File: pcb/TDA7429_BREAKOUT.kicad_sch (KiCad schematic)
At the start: 53 parts

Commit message: start redesigning schematic
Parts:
- removed AUDIO_IN: (no value), symbol pinhead:PINHD-2X6
- removed AUDIO_OUT: (no value), symbol pinhead:PINHD-2X4
- removed C1, C15, C17, C2: 22nF, symbol OPL Eagle Library:C*-0805
- removed C10, C8, C9: 2.2uF, symbol OPL Eagle Library:C*-0805
- removed C11, C12, C13, C14, C30, C4: 100nF, symbol OPL Eagle Library:C*-0805
- removed C16, C18: 18nF, symbol OPL Eagle Library:C*-0805
- removed C19, C20, C6: 5.6nF, symbol OPL Eagle Library:C*-0805
- removed C21: 22uF, symbol OPL Eagle Library:C*-0805
- removed C22, C23, C24, C25, C26, C27: 0.47uF, symbol OPL Eagle Library:C*-0805
- removed C3: 4.7nF, symbol OPL Eagle Library:C*-0805
- removed C31: 10uF, symbol OPL Eagle Library:C*-0805
- removed C5: 1.2nF, symbol OPL Eagle Library:C*-0805
- removed C7: 680nF, symbol OPL Eagle Library:C*-0805
- removed D1: (no value), symbol OPL Eagle Library:LED*
- removed DATA, POWER: (no value), symbol SparkFun-Connectors:M02PTH
- removed FRAME1 (x2): (no value), symbol SparkFun-Aesthetics:FRAME-LETTER
- removed GND1, GND10, GND11, GND12, GND13, GND14, GND15, GND17, GND20, GND21: (no value), symbol supply1:GND
- removed MONITOR: (no value), symbol pinhead:PINHD-2X2
- removed R1, R2: 5.6K, symbol OPL Eagle Library:R*-0603
- removed R3, R4: 2.7K, symbol OPL Eagle Library:R*-0603
- removed R5: 220, symbol OPL Eagle Library:R*-0603
- removed TDA7429S: (no value), symbol ATK_lib:TDA7429S_SURFACE
- added C1, C10, C11, C12, C13, C14, C15, C16, C17, C18, C19, C2, C20, C21, C22, C23, C24, C25, C26, C27, C28, C29, C3, C4, C5, C6, C7, C8, C9: 22nF, symbol Device:C_Small
- added R1, R2: 2.7K, symbol Device:R_Small
- added R3: R_Small, symbol Device:R_Small
- added R4: 5.6K, symbol Device:R_Small
- added U1: TDA7429S, TDA7429:SDIP-42_W15.24mm_P1.778mm, symbol TDA7429:TDA7429S_TC
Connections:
- new net: C16.1, C17.1, R4.1
- new net: C17.2, U1.15 (BASS_LO)
- new net: C19.2, C20.2, U1.42 (V_S)
- new net: C10.1, C9.1, R1.1
- new net: C9.2, U1.19 (MIDDLE_LO)
- new net: C11.1, C12.1, R2.1
- new net: C11.2, U1.21 (MIDDLE_RO)
- new net: C26.2, U1.40 (R_IN3)
- new net: C12.2, U1.22 (MIDDLE_RI)
- new net: C14.1, C15.1, R3.1
- new net: C16.2, U1.16 (BASS_LI)
- new net: C27.1, U1.10 (REARIN)
- new net: C27.2, U1.9 (REAROUT)
- new net: C29.1, U1.13 (VAR_R)
- new net: C29.2, U1.14 (BASSO_R)
- new net: C1.2, U1.1 (PS4)
- new net: C7.2, U1.23 (TREBLE_R)
- new net: C4.2, U1.4 (PS1)
- new net: C23.2, U1.35 (L_IN1)
- new net: C10.2, U1.20 (MIDDLE_LI)
- new net: C15.2, U1.17 (BASS_RO)
- new net: C18.2, U1.41 (CREF)
- new net: C8.2, U1.24 (TREBLE_L)
- new net: C14.2, U1.18 (BASS_RI)
- new net: C28.1, U1.11 (VAR_L)
- new net: C28.2, U1.12 (BASSO_L)
- new net: C2.2, U1.2 (PS3)
- new net: C3.2, U1.3 (PS2)
- new net: C21.2, U1.33 (L_IN3)
- new net: C22.2, U1.34 (L_IN2)
- new net: C24.2, U1.38 (R_IN1)
- new net: C25.2, U1.39 (R_IN2)
- new net: C5.2, U1.5 (LP)
- new net: C6.2, U1.6 (LP1)
- new net: C13.2, U1.7 (HP1)
- new net: C13.1, U1.8 (HP2)
- new net GNDA: C1.1, C18.1, C19.1, C2.1, C20.1, C3.1, C4.1, C5.1, C6.1, C7.1, C8.1, R1.2, R2.2, R3.2, R4.2, U1.25 (AGND)

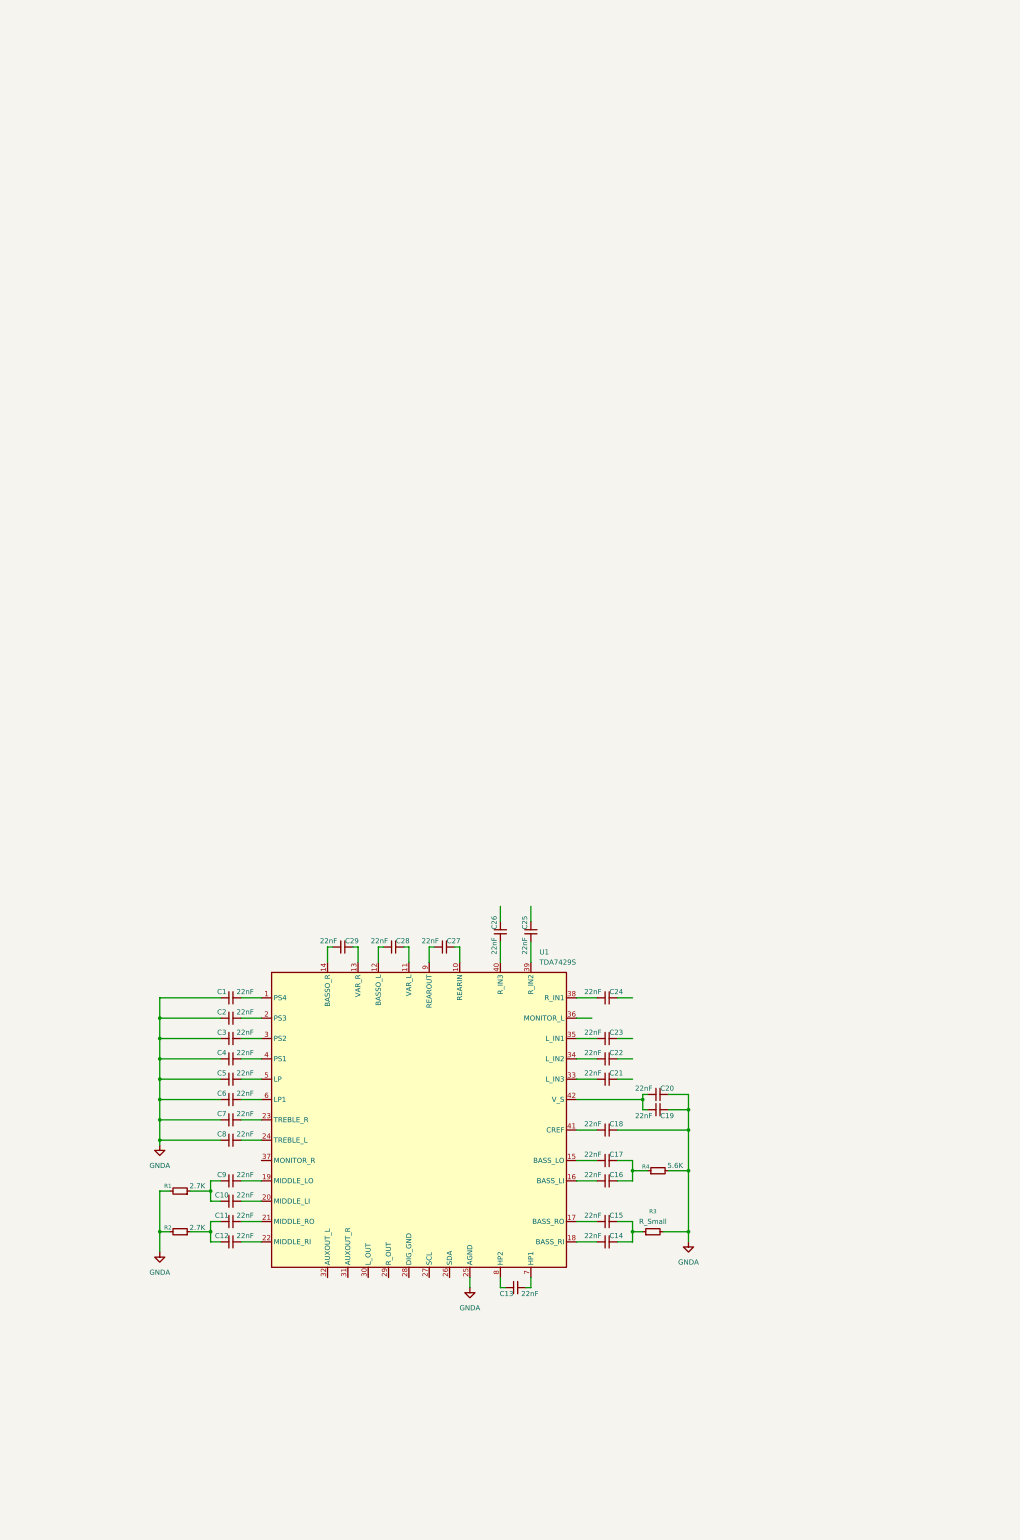
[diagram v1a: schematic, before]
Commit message: update schematic
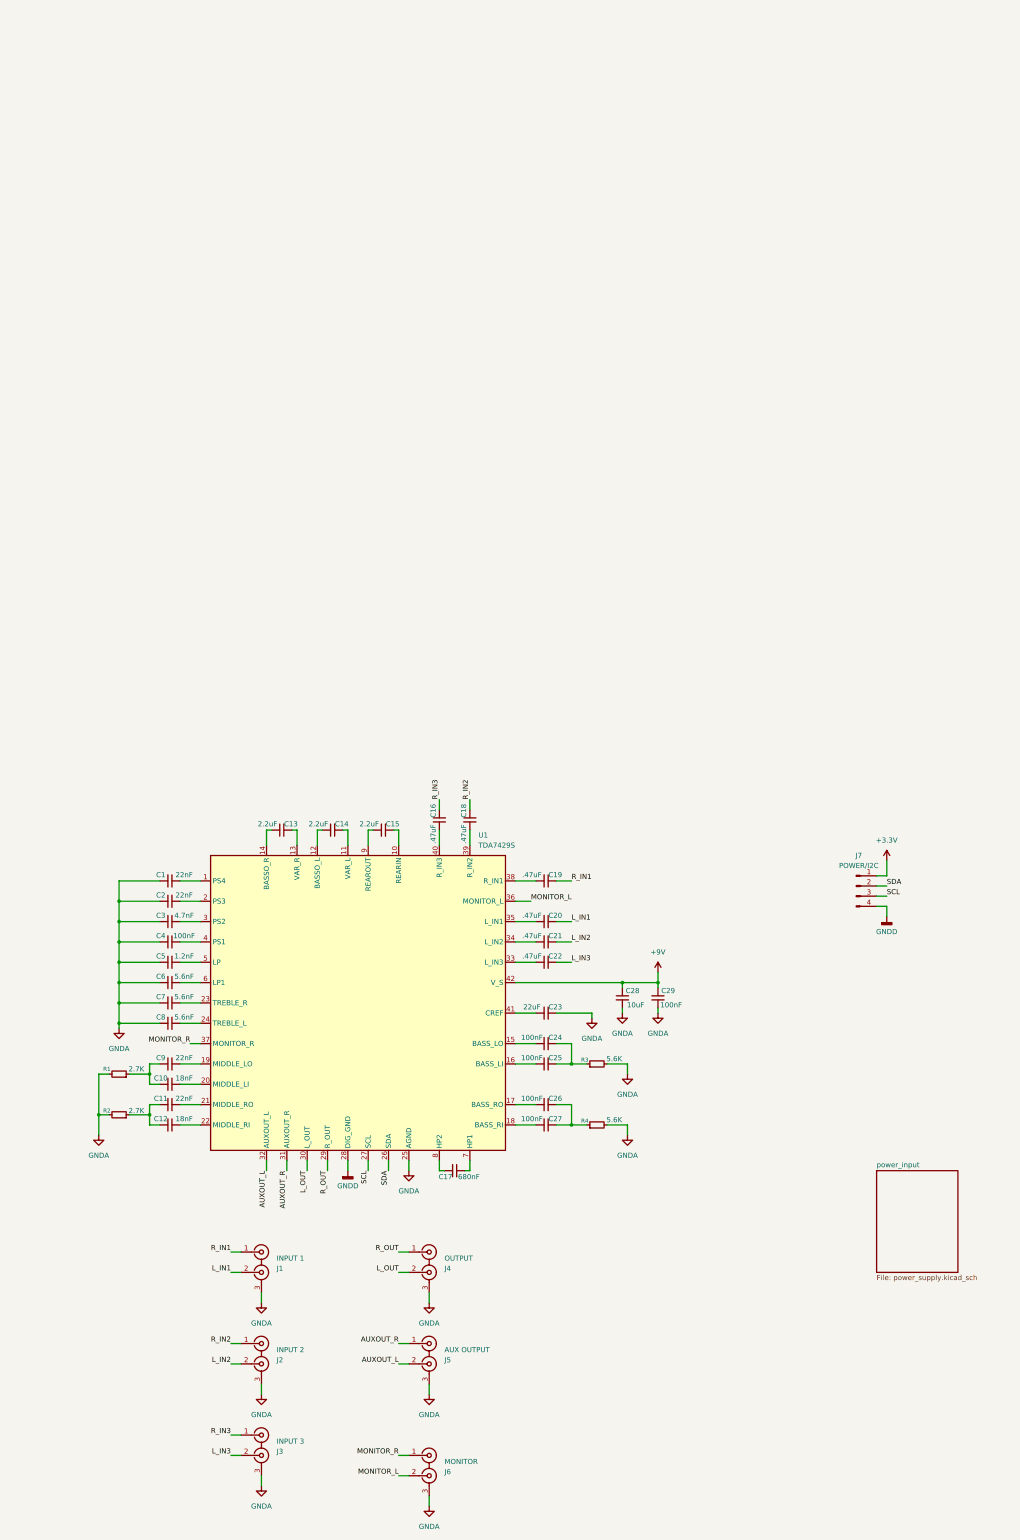
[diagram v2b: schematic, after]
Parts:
- added J1: INPUT 1, symbol Connector:Conn_Coaxial_x2
- added J2: INPUT 2, symbol Connector:Conn_Coaxial_x2
- added J3: INPUT 3, symbol Connector:Conn_Coaxial_x2
- added J4: OUTPUT, symbol Connector:Conn_Coaxial_x2
- added J5: AUX OUTPUT, symbol Connector:Conn_Coaxial_x2
- added J6: MONITOR, symbol Connector:Conn_Coaxial_x2
- added J7: POWER/I2C, symbol Connector:Conn_01x04_Pin
- C10, C12: value 22nF -> 18nF
- C13: renamed from C29; value 22nF -> 2.2uF
- C14: renamed from C28; value 22nF -> 2.2uF
- C15: renamed from C27; value 22nF -> 2.2uF
- C16: renamed from C26; value 22nF -> .47uF
- C17: renamed from C13; value 22nF -> 680nF
- C18: renamed from C25; value 22nF -> .47uF
- C19: renamed from C24; value 22nF -> .47uF
- C20: renamed from C23; value 22nF -> .47uF
- C21: renamed from C22; value 22nF -> .47uF
- C22: renamed from C21; value 22nF -> .47uF
- C23: renamed from C18; value 22nF -> 22uF
- C24: renamed from C17; value 22nF -> 100nF
- C25: renamed from C16; value 22nF -> 100nF
- C26: renamed from C15; value 22nF -> 100nF
- C27: renamed from C14; value 22nF -> 100nF
- C28: renamed from C19; value 22nF -> 10uF
- C29: renamed from C20; value 22nF -> 100nF
- C3: value 22nF -> 4.7nF
- C4: value 22nF -> 100nF
- C5: value 22nF -> 1.2nF
- C6, C7, C8: value 22nF -> 5.6nF
- R4: renamed from R3; value R_Small -> 5.6K
- renumbered R4 to R3
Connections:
- net GNDA: now also C28.2, C29.2, J1.3 (EXT), J2.3 (EXT), J3.3 (EXT), J4.3 (EXT), J5.3 (EXT), J6.3 (EXT); no longer C28.1, C29.1
- net R_IN3: now reaches C16.1
- net R_IN3: now also J3.1 (IN1)
- net L_IN1: now reaches C20.1
- net L_IN1: now also J1.2 (IN2)
- net SDA: now reaches U1.26 (SDA)
- net SDA: now also J7.2 (Pin_2)
- net SCL: now reaches U1.27 (SCL)
- net SCL: now also J7.3 (Pin_3)
- net GNDD: now reaches U1.28 (DIG_GND)
- net GNDD: now also J7.4 (Pin_4)
- net R_OUT: now reaches U1.29 (R_OUT)
- net R_OUT: now also J4.1 (IN1)
- net L_OUT: now reaches U1.30 (L_OUT)
- net L_OUT: now also J4.2 (IN2)
- net AUXOUT_R: now reaches U1.31 (AUXOUT_R)
- net AUXOUT_R: now also J5.1 (IN1)
- net AUXOUT_L: now reaches U1.32 (AUXOUT_L)
- net AUXOUT_L: now also J5.2 (IN2)
- net MONITOR_L: now reaches U1.36 (MONITOR_L)
- net MONITOR_L: now also J6.2 (IN2)
- net MONITOR_R: now reaches U1.37 (MONITOR_R)
- net MONITOR_R: now also J6.1 (IN1)
- net L_IN3: now reaches C22.1
- net L_IN3: now also J3.2 (IN2)
- net R_IN1: now reaches C19.1
- net R_IN1: now also J1.1 (IN1)
- net R_IN2: now reaches C18.1
- net R_IN2: now also J2.1 (IN1)
- net L_IN2: now reaches C21.1
- net L_IN2: now also J2.2 (IN2)
- new net +3.3V: J7.1 (Pin_1)
- new net +9V: C28.1, C29.1, U1.42 (V_S)
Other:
- added sheet power_input (power_supply.kicad_sch)
- title: (none) -> TDA7429S Breakout Board with Automotive Grade Power Supply
- moved on the sheet: C1, C10, C11, C12, C13, C14, C15, C16, C17, C18, C19, C2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

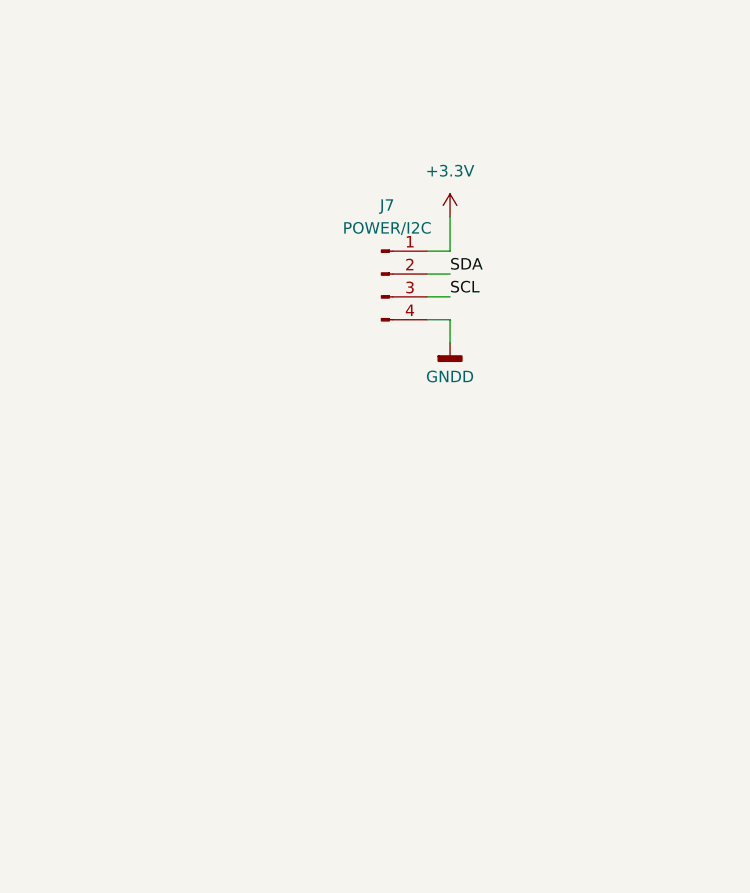
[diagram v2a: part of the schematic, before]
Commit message: tweak schematic, add i2c pullup resistors.
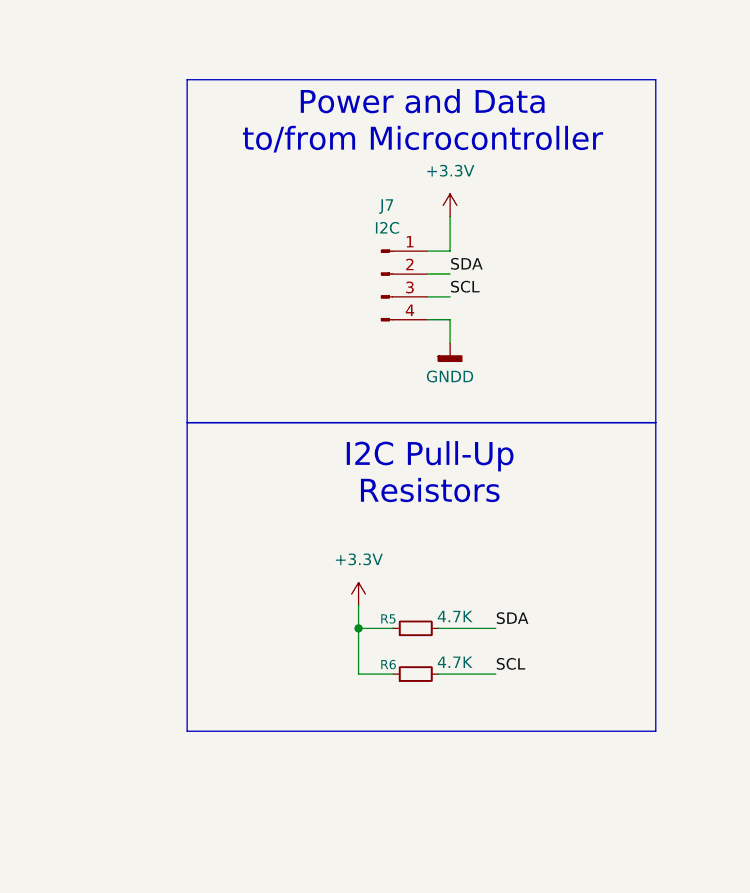
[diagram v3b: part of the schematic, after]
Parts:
- added R5, R6: 4.7K, symbol Device:R_Small
- C1, C10, C11, C12, C13, C14, C15, C16, C17, C18, C19, C2, C20, C21, C22, C23, C24, C25, C26, C27, C28, C29, C3, C4, C5, C6, C7, C8, C9: footprint (none) -> Capacitor_SMD:C_0805_2012Metric_Pad1.18x1.45mm_HandSolder
- J7: value POWER/I2C -> I2C
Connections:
- net +3.3V: now also R5.1, R6.1
- net SCL: now also R6.2
- net SDA: now also R5.2
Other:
- note added: "I2C Pull-Up Resistors"
- note added: "Power and Data to/from Microcontroller"
